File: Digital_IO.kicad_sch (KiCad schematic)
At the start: 16 parts, among them J1 MMCX, J10 MMCX, J11 MMCX, J12 MMCX, J13 MMCX, J14 MMCX, J15 MMCX, J16 MMCX, J2 MMCX, J3 MMCX, J4 MMCX, J5 MMCX, J6 MMCX, J7 MMCX, J8 MMCX, J9 MMCX

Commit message: Final Draft - Ready for review
Updates:
- Changed area behind FMC connector to match the new Osprey FMC template
  - This includes a new 12V LED, more robust power input traces, arranged elements for readability.

Things to do:
Round diff traces before generating fabrication files
Change name of project to 'trigger output fmc'
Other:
- title: FMC Template -> Trigger Output FMC
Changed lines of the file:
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@@
 	(paper "A4")
 	(title_block
-		(title "FMC Template")
-		(date "2026-01-26")
+		(title "Trigger Output FMC")
+		(date "2026-05-07")
 		(rev "1.0")
 		(company "SPDX-FileCopyrightText: 2025 Osprey DCS")

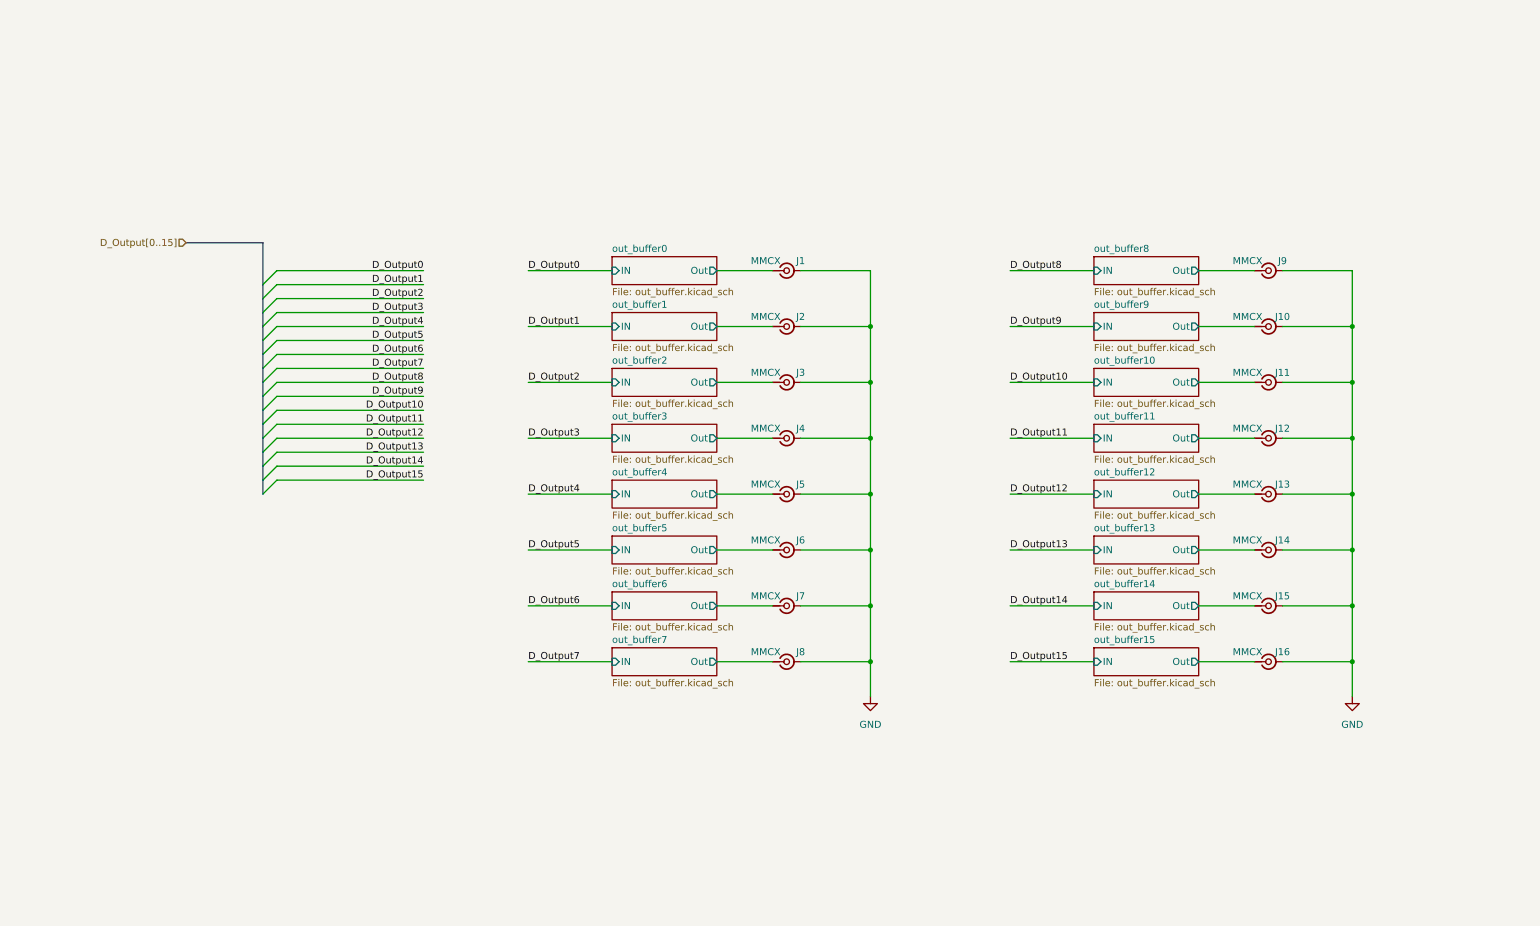
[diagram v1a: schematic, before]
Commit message: Changed Trigger Outputs Topology
- Changed to a comp to digital TX design
- Added power section to support this change
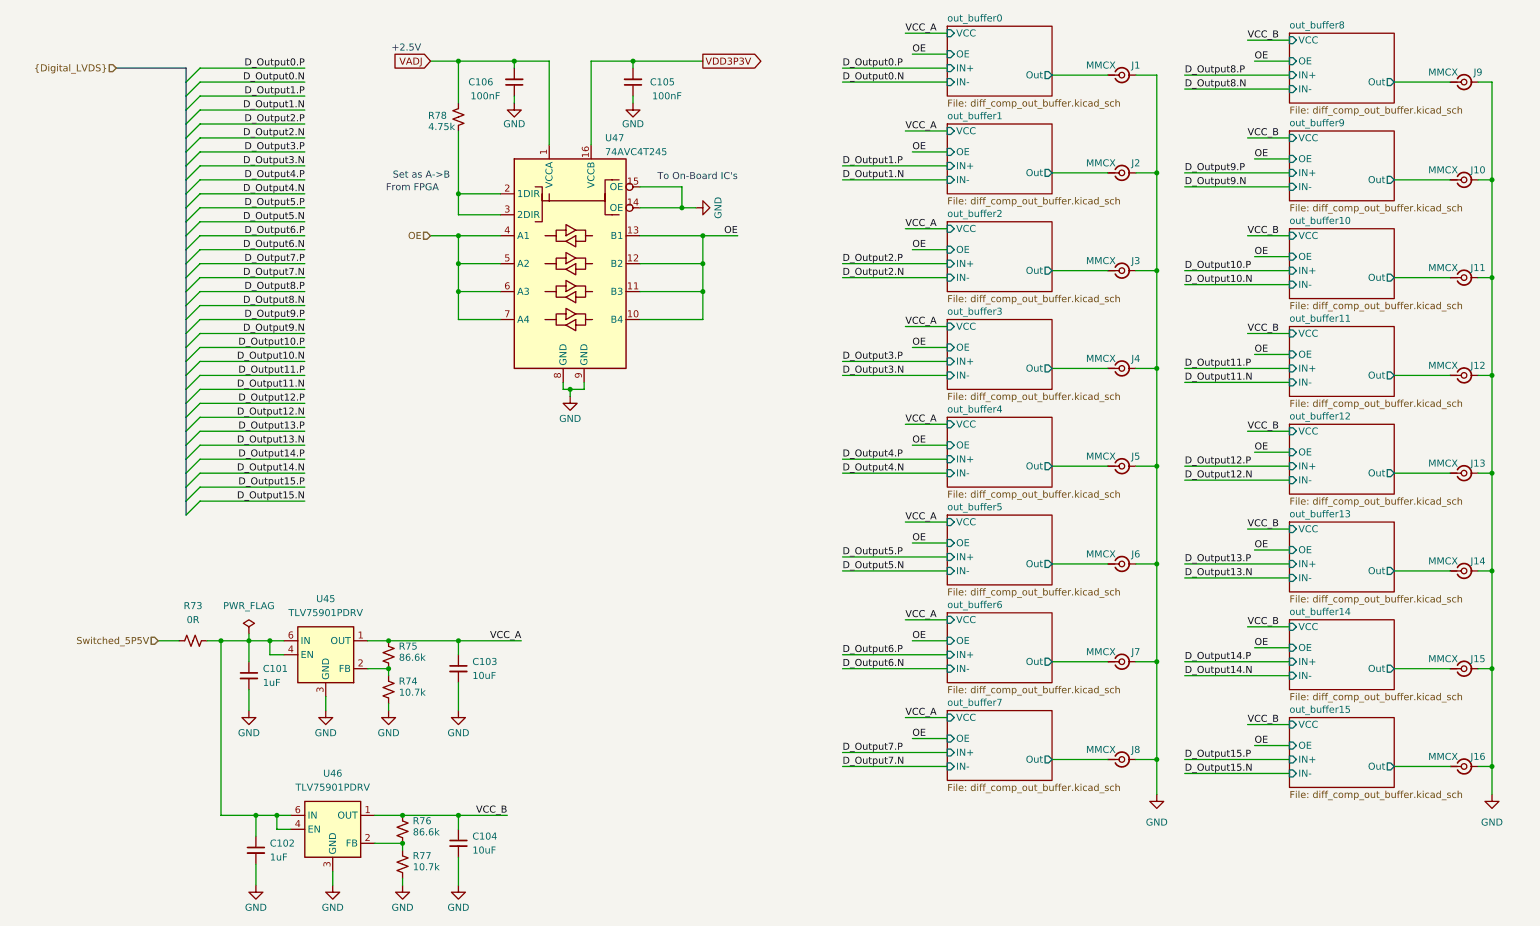
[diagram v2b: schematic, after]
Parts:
- added C101, C102: 1uF, Capacitor_SMD:C_0603_1608Metric, symbol Device:C_Small
- added C103, C104: 10uF, Capacitor_SMD:C_0805_2012Metric, symbol Device:C_Small
- added C105, C106: 100nF, Capacitor_SMD:C_0402_1005Metric, symbol Device:C_Small
- added R73: 0R, Resistor_SMD:R_0603_1608Metric, symbol Device:R_Small_US
- added R74, R77: 10.7k, Resistor_SMD:R_0402_1005Metric, symbol Device:R_Small_US
- added R75, R76: 86.6k, Resistor_SMD:R_0402_1005Metric, symbol Device:R_Small_US
- added R78: 4.75k, Resistor_SMD:R_0402_1005Metric, symbol Device:R_Small_US
- added U45, U46: TLV75901PDRV, Package_SON:WSON-6-1EP_2x2mm_P0.65mm_EP1x1.6mm, symbol Regulator_Linear:TLV75801PDRV
- added U47: 74AVC4T245, Package_SO:TSSOP-16_4.4x5mm_P0.65mm, symbol evr-fmc:74LVC4T245
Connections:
- net GND: now also C101.2, C102.2, C103.2, C104.2, C105.1, C106.1, R74.1, R77.1, U45.3 (GND), U45.7 (GND), U46.3 (GND), U46.7 (GND), U47.14 (OE), U47.15 (OE), U47.8 (GND), U47.9 (GND)
- new net: R78.1, U47.2 (1DIR), U47.3 (2DIR)
- new net: R74.2, R75.1, U45.2 (FB)
- new net: R76.1, R77.2, U46.2 (FB)
- new net: C101.1, C102.1, R73.2, U45.4 (EN), U45.6 (IN), U46.4 (EN), U46.6 (IN)
- new net OE: U47.10 (B4), U47.11 (B3), U47.12 (B2), U47.13 (B1), U47.4 (A1), U47.5 (A2), U47.6 (A3), U47.7 (A4)
- new net Switched_5P5V: R73.1
- new net VADJ: C106.2, R78.2, U47.1 (VCCA)
- new net VCC_A: C103.1, R75.2, U45.1 (OUT)
- new net VCC_B: C104.1, R76.2, U46.1 (OUT)
- new net VDD3P3V: C105.2, U47.16 (VCCB)
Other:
- sheet out_buffer0: file out_buffer.kicad_sch -> diff_comp_out_buffer.kicad_sch
- sheet out_buffer0 ports: added IN+, IN-, OE, VCC; removed IN
- sheet out_buffer1: file out_buffer.kicad_sch -> diff_comp_out_buffer.kicad_sch
- sheet out_buffer1 ports: added IN+, IN-, OE, VCC; removed IN
- sheet out_buffer10: file out_buffer.kicad_sch -> diff_comp_out_buffer.kicad_sch
- sheet out_buffer10 ports: added IN+, IN-, OE, VCC; removed IN
- sheet out_buffer11: file out_buffer.kicad_sch -> diff_comp_out_buffer.kicad_sch
- sheet out_buffer11 ports: added IN+, IN-, OE, VCC; removed IN
- sheet out_buffer12: file out_buffer.kicad_sch -> diff_comp_out_buffer.kicad_sch
- sheet out_buffer12 ports: added IN+, IN-, OE, VCC; removed IN
- sheet out_buffer13: file out_buffer.kicad_sch -> diff_comp_out_buffer.kicad_sch
- sheet out_buffer13 ports: added IN+, IN-, OE, VCC; removed IN
- sheet out_buffer14: file out_buffer.kicad_sch -> diff_comp_out_buffer.kicad_sch
- sheet out_buffer14 ports: added IN+, IN-, OE, VCC; removed IN
- sheet out_buffer15: file out_buffer.kicad_sch -> diff_comp_out_buffer.kicad_sch
- sheet out_buffer15 ports: added IN+, IN-, OE, VCC; removed IN
- sheet out_buffer2: file out_buffer.kicad_sch -> diff_comp_out_buffer.kicad_sch
- sheet out_buffer2 ports: added IN+, IN-, OE, VCC; removed IN
- sheet out_buffer3: file out_buffer.kicad_sch -> diff_comp_out_buffer.kicad_sch
- sheet out_buffer3 ports: added IN+, IN-, OE, VCC; removed IN
- sheet out_buffer4: file out_buffer.kicad_sch -> diff_comp_out_buffer.kicad_sch
- sheet out_buffer4 ports: added IN+, IN-, OE, VCC; removed IN
- sheet out_buffer5: file out_buffer.kicad_sch -> diff_comp_out_buffer.kicad_sch
- sheet out_buffer5 ports: added IN+, IN-, OE, VCC; removed IN
- sheet out_buffer6: file out_buffer.kicad_sch -> diff_comp_out_buffer.kicad_sch
- sheet out_buffer6 ports: added IN+, IN-, OE, VCC; removed IN
- sheet out_buffer7: file out_buffer.kicad_sch -> diff_comp_out_buffer.kicad_sch
- sheet out_buffer7 ports: added IN+, IN-, OE, VCC; removed IN
- sheet out_buffer8: file out_buffer.kicad_sch -> diff_comp_out_buffer.kicad_sch
- sheet out_buffer8 ports: added IN+, IN-, OE, VCC; removed IN
- sheet out_buffer9: file out_buffer.kicad_sch -> diff_comp_out_buffer.kicad_sch
- sheet out_buffer9 ports: added IN+, IN-, OE, VCC; removed IN
- note added: "+2.5V"
- note added: "From FPGA"
- note added: "Set as A->B"
- note added: "To On-Board IC's"
- moved on the sheet: J1, J10, J11, J12, J13, J14, J15, J16, J2, J3, J4, J5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

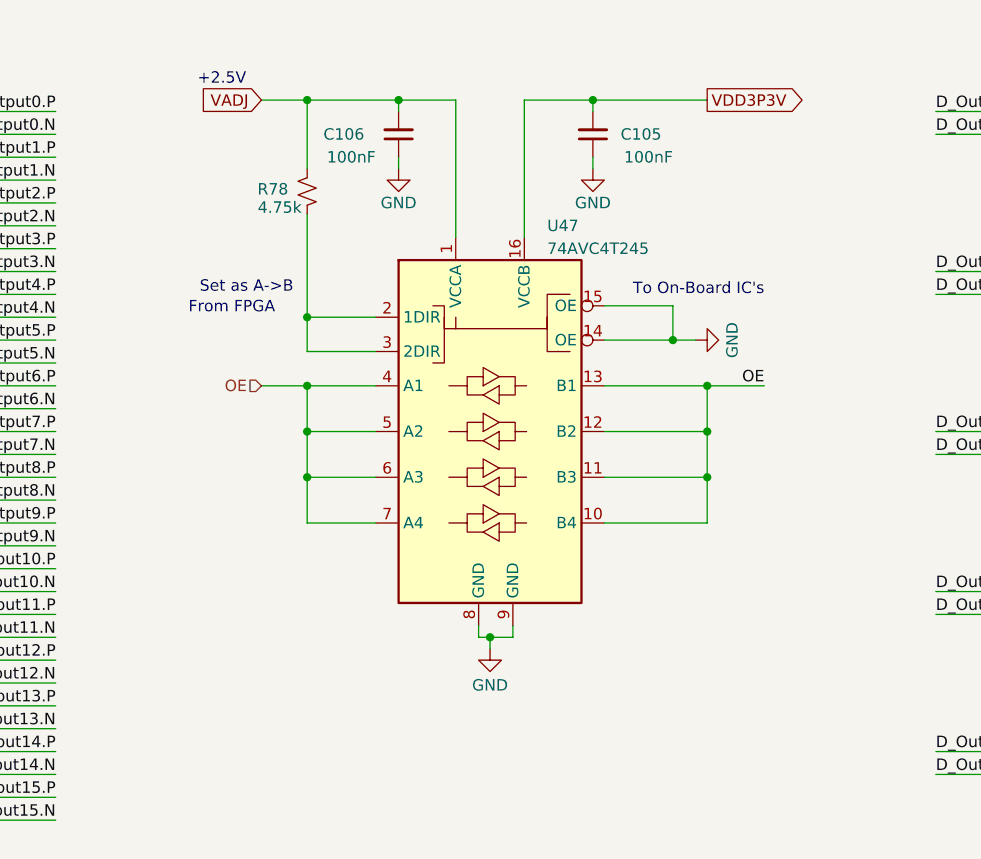
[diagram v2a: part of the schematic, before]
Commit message: Updated Layout - roughly floor planed all parts on board
- All parts fit on the board but routing may still result in power sections moving
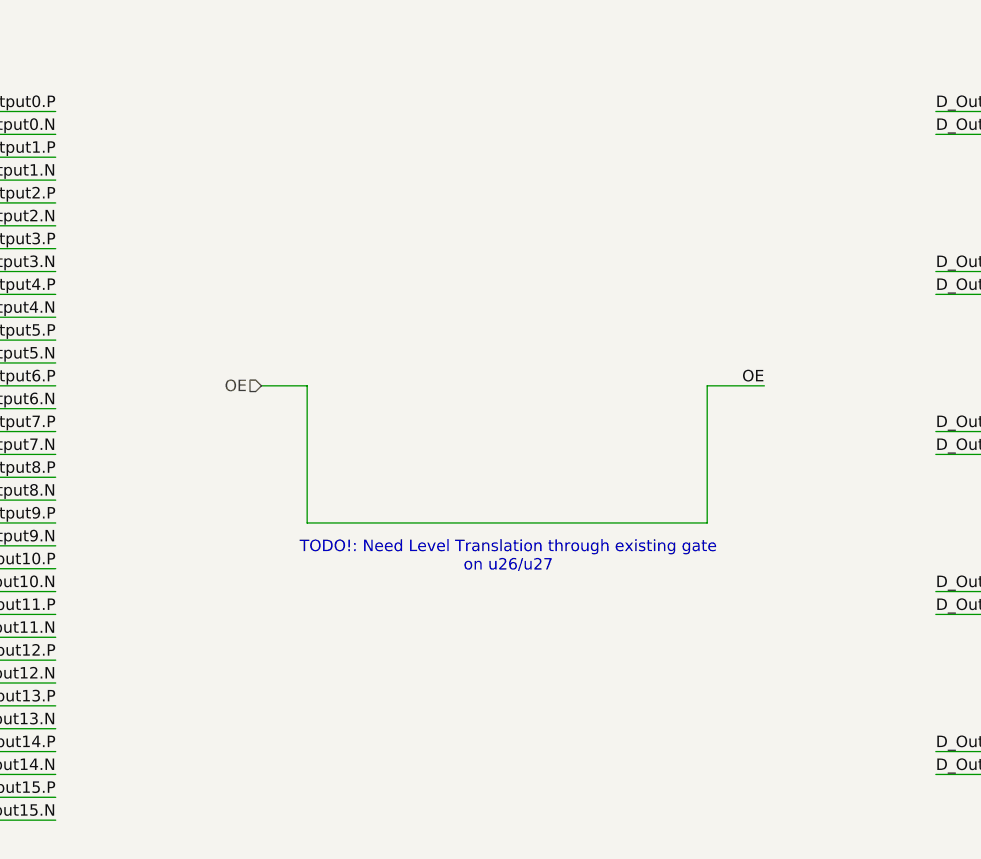
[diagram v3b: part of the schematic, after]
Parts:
- removed C105, C106: 100nF, Capacitor_SMD:C_0402_1005Metric, symbol Device:C_Small
- removed R78: 4.75k, Resistor_SMD:R_0402_1005Metric, symbol Device:R_Small_US
- removed U47: 74AVC4T245, Package_SO:TSSOP-16_4.4x5mm_P0.65mm, symbol evr-fmc:74LVC4T245
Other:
- note added: "TODO!: Need Level Translation through existing gate on u26/u27"
- note removed: "+2.5V"
- note removed: "From FPGA"
- note removed: "Set as A->B"
- note removed: "To On-Board IC's"
